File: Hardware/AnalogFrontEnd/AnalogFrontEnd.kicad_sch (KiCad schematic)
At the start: 0 parts

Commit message: simulate tia and improve docs
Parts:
- added C3, C4: 1u, Capacitor_SMD:C_0805_2012Metric, symbol Device:C
- added U2: AP2112K-3.3, Package_TO_SOT_SMD:SOT-23-5, symbol Regulator_Linear:AP2112K-3.3
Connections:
- new net +5V: C4.1, U2.1 (VIN), U2.3 (EN)
- new net GND: C3.2, C4.2, U2.2 (GND)
- new net SENSOR_VCC: C3.1, U2.5 (VOUT)
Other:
- added sheet Amplifier (Amplifier.kicad_sch)
- added sheet BiasSupply (BiasSupply.kicad_sch)
- added sheet ExternalConnector (ExternalConnector.kicad_sch)
- added sheet PulseShaping (PulseShaping.kicad_sch)
- added sheet SensorProtection (SensorProtection.kicad_sch)
- note added: "Enable pin where to connect name it sensor bias or sth the sheeet"

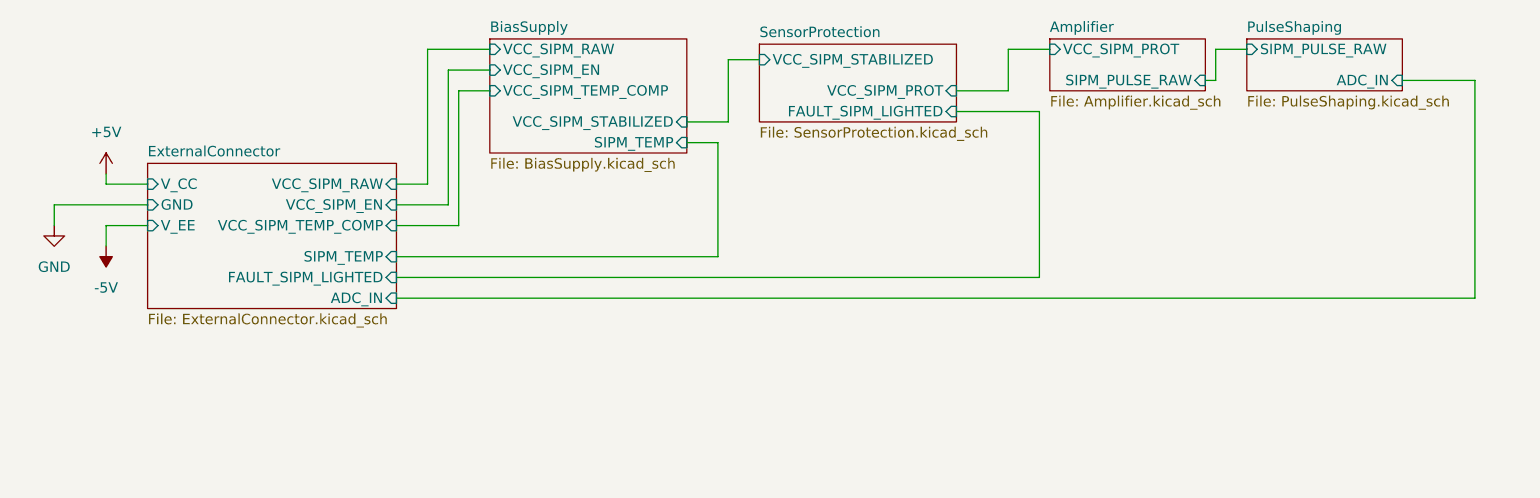
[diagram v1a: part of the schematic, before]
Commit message: add bias supply circuit
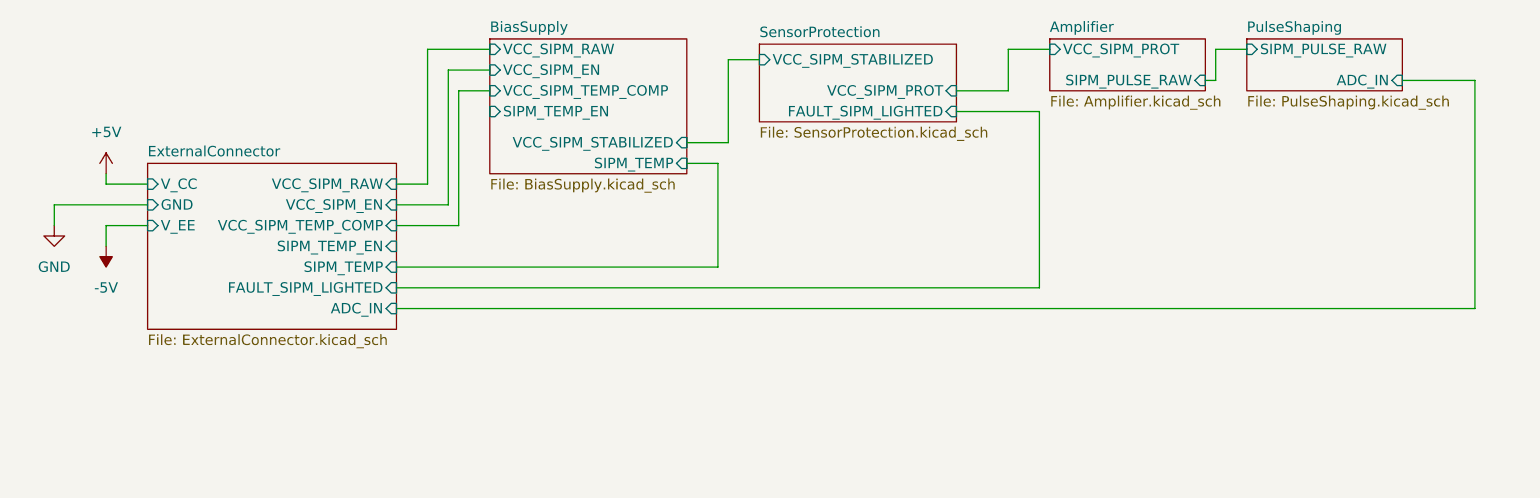
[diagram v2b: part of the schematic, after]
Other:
- sheet BiasSupply ports: added SIPM_TEMP_EN; removed none
- sheet ExternalConnector ports: added SIPM_TEMP_EN; removed none
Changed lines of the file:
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@@
 	(wire
 		(pts
-			(xy 170.18 67.31) (xy 170.18 46.99)
-		)
-		(stroke
-			(width 0)
-			(type default)
-		)
-	)
-	(wire
-		(pts
-			(xy 91.44 64.77) (xy 130.81 64.77)
+			(xy 170.18 68.58) (xy 170.18 46.99)
+		)
+		(stroke
+			(width 0)
+			(type default)
+		)
+	)
+	(wire
+		(pts
+			(xy 91.44 66.04) (xy 130.81 66.04)
 		)
 		(stroke
@@
 	(wire
 		(pts
-			(xy 130.81 50.8) (xy 127 50.8)
+			(xy 130.81 53.34) (xy 127 53.34)
 		)
 		(stroke
@@
 	(wire
 		(pts
-			(xy 127 48.26) (xy 132.08 48.26)
+			(xy 127 50.8) (xy 132.08 50.8)
 		)
 		(stroke
@@
 	(wire
 		(pts
-			(xy 130.81 64.77) (xy 130.81 50.8)
+			(xy 130.81 66.04) (xy 130.81 53.34)
 		)
 		(stroke
@@
 	(wire
 		(pts
-			(xy 132.08 48.26) (xy 132.08 40.64)
-		)
-		(stroke
-			(width 0)
-			(type default)
-		)
-	)
-	(wire
-		(pts
-			(xy 91.44 69.85) (xy 223.52 69.85)
+			(xy 132.08 50.8) (xy 132.08 40.64)
+		)
+		(stroke
+			(width 0)
+			(type default)
+		)
+	)
+	(wire
+		(pts
+			(xy 91.44 71.12) (xy 223.52 71.12)
 		)
 		(stroke
@@
 	(wire
 		(pts
-			(xy 223.52 43.18) (xy 223.52 69.85)
+			(xy 223.52 43.18) (xy 223.52 71.12)
 		)
 		(stroke
@@
 	(wire
 		(pts
-			(xy 91.44 67.31) (xy 170.18 67.31)
+			(xy 91.44 68.58) (xy 170.18 68.58)
 		)
 		(stroke
@@
 	(sheet
 		(at 102.87 38.1)
-		(size 24.13 13.97)
+		(size 24.13 16.51)
 		(exclude_from_sim no)
 		(in_bom yes)
@@
 		)
 		(property "Sheetfile" "BiasSupply.kicad_sch"
-			(at 102.87 52.6546 0)
+			(at 102.87 55.1946 0)
 			(show_name no)
 			(do_not_autoplace no)
@@
 		)
 		(pin "VCC_SIPM_STABILIZED" input
-			(at 127 48.26 0)
+			(at 127 50.8 0)
 			(effects
 				(font
@@
 		)
 		(pin "SIPM_TEMP" input
-			(at 127 50.8 0)
+			(at 127 53.34 0)
 			(effects
 				(font
@@
 				)
 				(justify right)
+			)
+		)
+		(pin "SIPM_TEMP_EN" input
+			(at 102.87 46.99 180)
+			(effects
+				(font
+					(size 1.27 1.27)
+				)
+				(justify left)
 			)
 		)
@@
 	(sheet
 		(at 60.96 53.34)
-		(size 30.48 17.78)
+		(size 30.48 20.32)
 		(exclude_from_sim no)
 		(in_bom yes)
@@
 		)
 		(property "Sheetfile" "ExternalConnector.kicad_sch"
-			(at 60.96 71.7046 0)
+			(at 60.96 74.2446 0)
 			(show_name no)
 			(do_not_autoplace no)
@@
 		)
 		(pin "FAULT_SIPM_LIGHTED" input
-			(at 91.44 67.31 0)
+			(at 91.44 68.58 0)
 			(effects
 				(font
@@
 		)
 		(pin "ADC_IN" input
-			(at 91.44 69.85 0)
+			(at 91.44 71.12 0)
 			(effects
 				(font
@@
 		)
 		(pin "SIPM_TEMP" input
-			(at 91.44 64.77 0)
+			(at 91.44 66.04 0)
 			(effects
 				(font
@@
 			(effects
 				(font
+					(size 1.27 1.27)
+				)
+				(justify right)
+			)
+		)
+		(pin "SIPM_TEMP_EN" input
+			(at 91.44 63.5 0)
+			(effects
+				(font

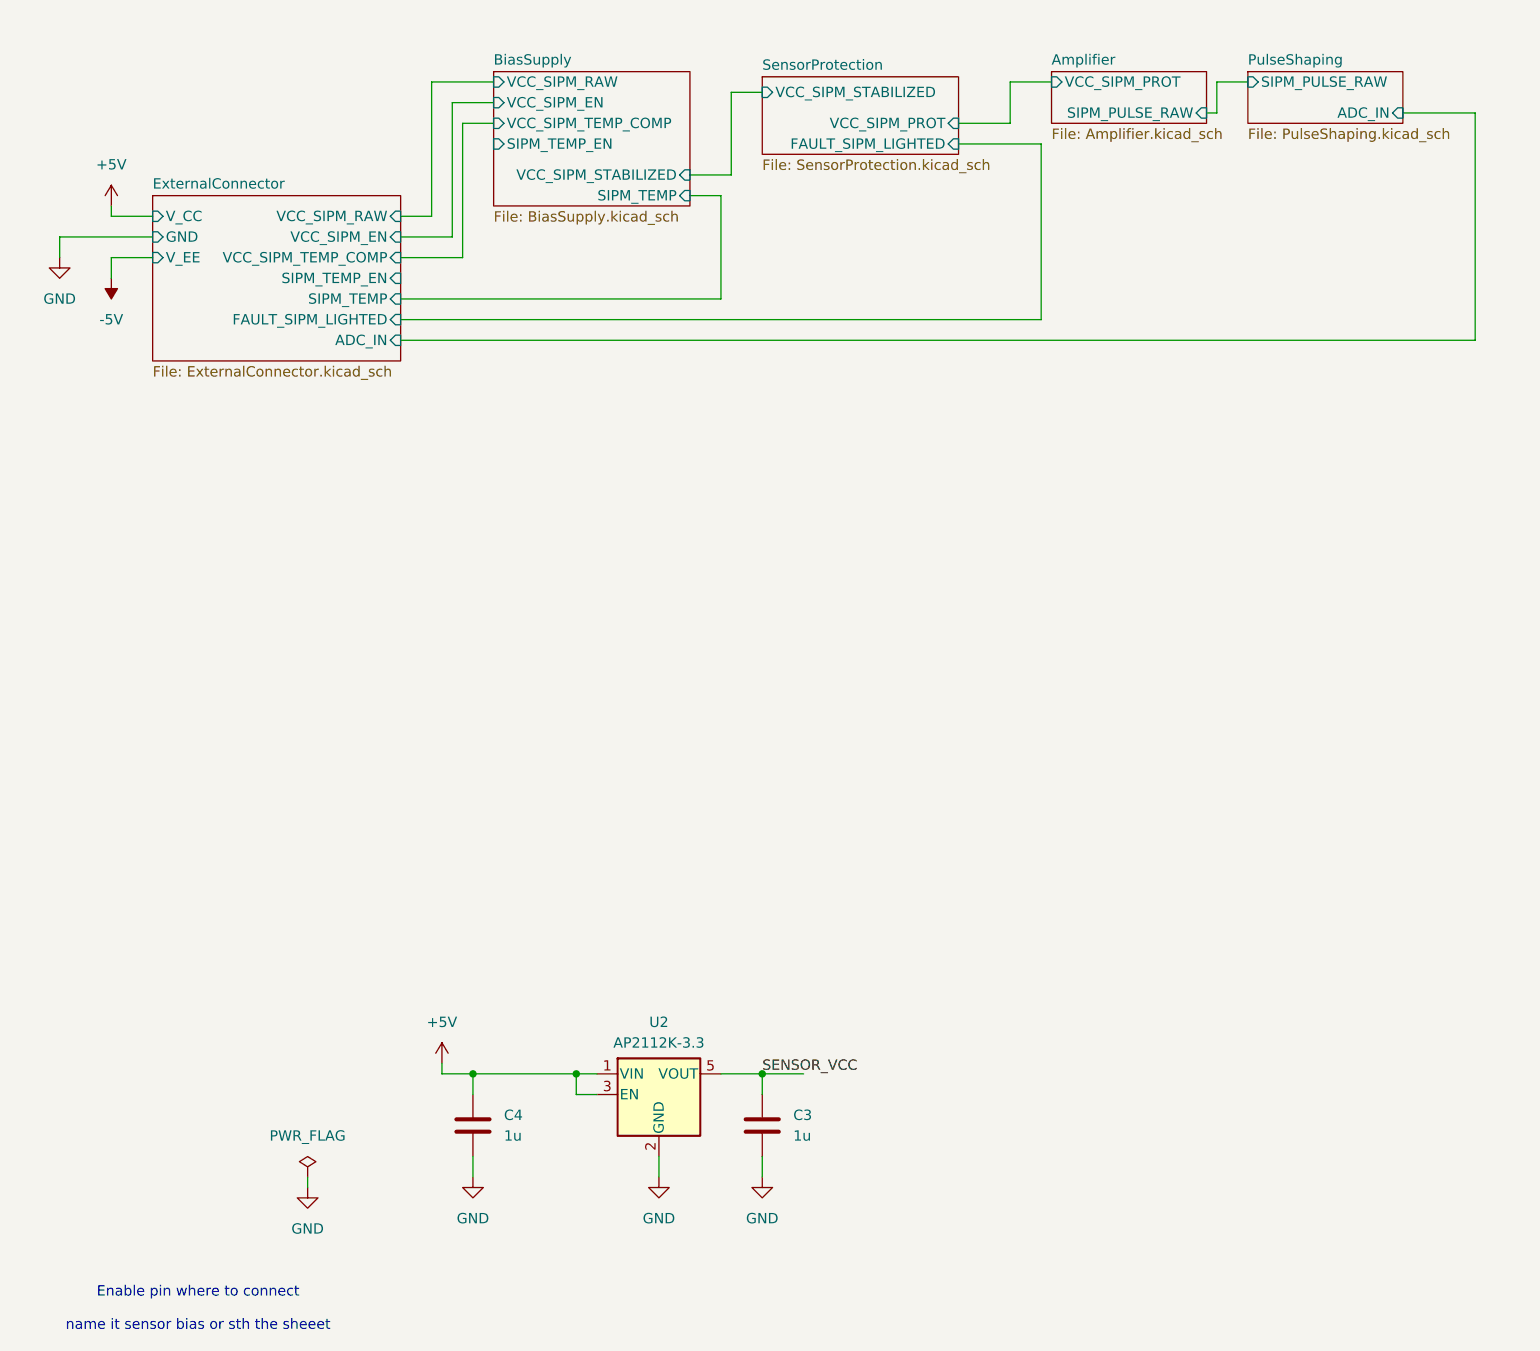
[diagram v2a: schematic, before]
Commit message: add draft of data processing circuit
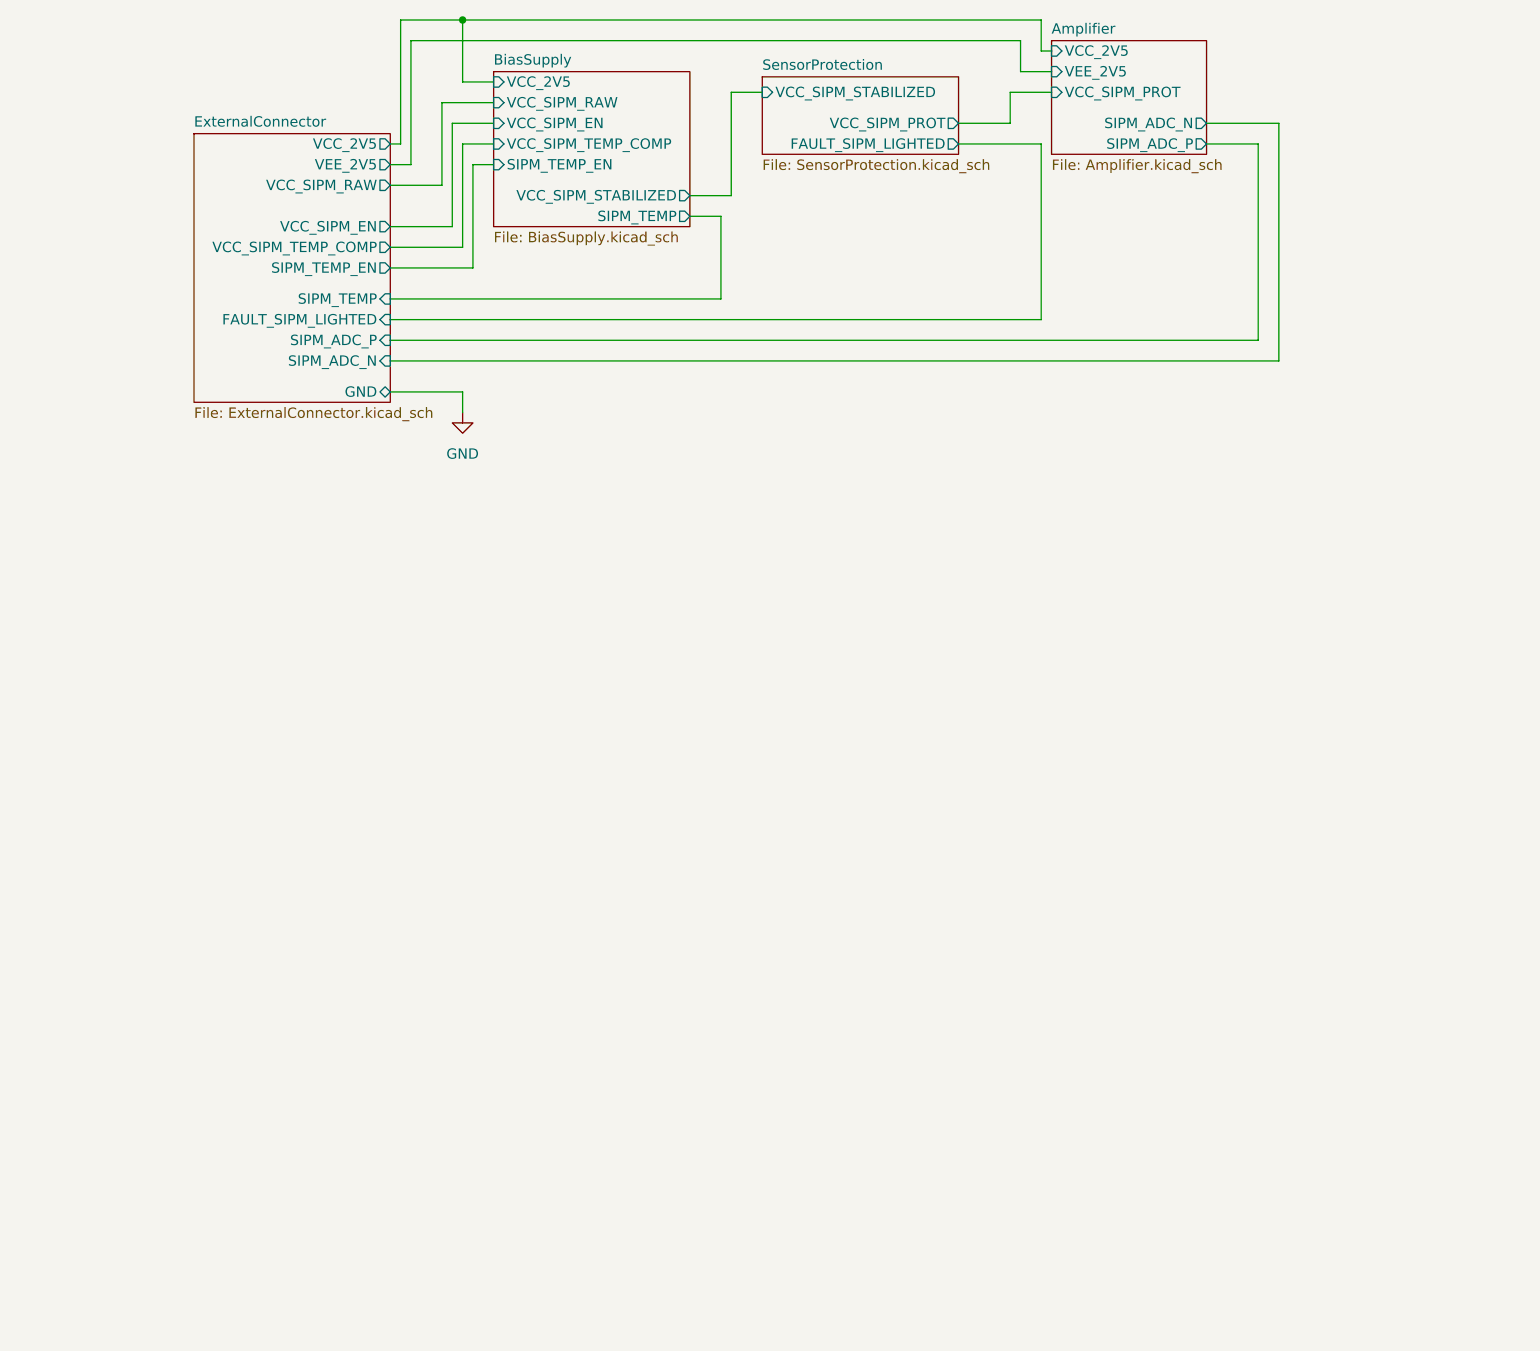
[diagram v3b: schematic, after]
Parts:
- removed C3, C4: 1u, Capacitor_SMD:C_0805_2012Metric, symbol Device:C
- removed U2: AP2112K-3.3, Package_TO_SOT_SMD:SOT-23-5, symbol Regulator_Linear:AP2112K-3.3
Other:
- removed sheet PulseShaping
- sheet Amplifier ports: added SIPM_ADC_N, SIPM_ADC_P, VCC_2V5, VEE_2V5; removed SIPM_PULSE_RAW
- sheet BiasSupply ports: added VCC_2V5; removed none
- sheet ExternalConnector ports: added SIPM_ADC_N, SIPM_ADC_P, VCC_2V5, VEE_2V5; removed ADC_IN, V_CC, V_EE
- note removed: "Enable pin where to connect name it sensor bias or sth the sheeet"
